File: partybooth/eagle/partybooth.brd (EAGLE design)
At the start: 61.6 x 39 mm, 26 parts, among them IC1 TINY13-20PU, IC2 78L05Z, J1 Lamp, J2 Button, J3 12V, T1 2N3904, T2 2N3904, X1 1501_06

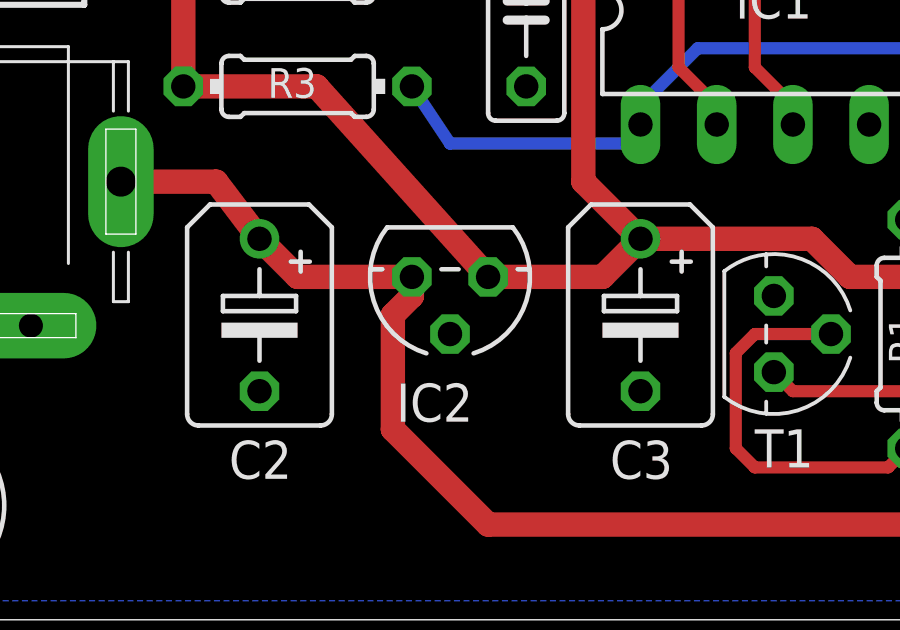
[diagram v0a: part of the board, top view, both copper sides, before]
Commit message: 
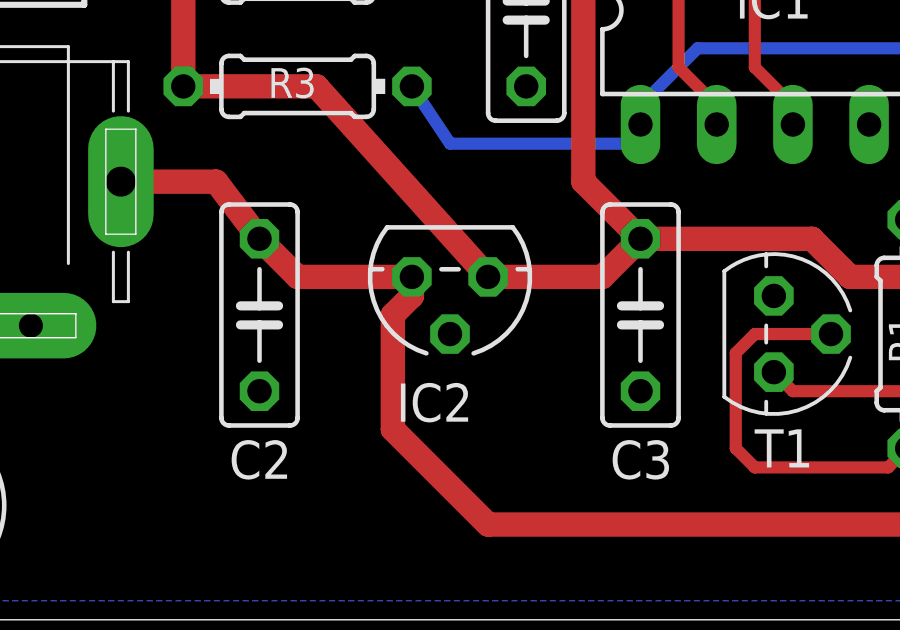
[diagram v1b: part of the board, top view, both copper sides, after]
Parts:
- C2: value 100u -> 0.33u; device rcl:B45181B -> rcl:C050-025X075
- C3: value 10u -> 0.1u; device rcl:B45181B -> rcl:C050-025X075
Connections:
- net +12V: now also C2.1; no longer C2.+
- net +5V: now also C3.1; no longer C3.+
- net GND: now also C2.2, C3.2; no longer C2.-, C3.-
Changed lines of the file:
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@@
 <attribute name="NAME" x="22.352" y="7.874" size="1.27" layer="25" ratio="10" rot="R180"/>
 </element>
-<element name="C2" library="rcl" package="B45181B" value="100u" x="15.24" y="10.16" smashed="yes" rot="R270">
+<element name="C2" library="rcl" package="C050-025X075" value="0.33u" x="15.24" y="10.16" smashed="yes" rot="R270">
 <attribute name="NAME" x="14.224" y="4.699" size="1.27" layer="25" ratio="10"/>
 </element>
-<element name="C3" library="rcl" package="B45181B" value="10u" x="27.94" y="10.16" smashed="yes" rot="R270">
+<element name="C3" library="rcl" package="C050-025X075" value="0.1u" x="27.94" y="10.16" smashed="yes" rot="R270">
 <attribute name="NAME" x="26.924" y="4.699" size="1.27" layer="25" ratio="10"/>
 </element>
@@
 <contactref element="OK1" pad="2"/>
 <contactref element="OK1" pad="3"/>
-<contactref element="C2" pad="-"/>
-<contactref element="C3" pad="-"/>
+<contactref element="C2" pad="2"/>
+<contactref element="C3" pad="2"/>
 <contactref element="IC2" pad="2"/>
 <contactref element="J3" pad="1"/>
@@
 <contactref element="SV1" pad="2"/>
 <contactref element="C1" pad="1"/>
-<contactref element="C3" pad="+"/>
+<contactref element="C3" pad="1"/>
 <contactref element="IC2" pad="1"/>
 <contactref element="R4" pad="2"/>
@@
 <signal name="+12V">
 <contactref element="J1" pad="1"/>
-<contactref element="C2" pad="+"/>
+<contactref element="C2" pad="1"/>
 <contactref element="IC2" pad="3"/>
 <contactref element="J3" pad="3"/>

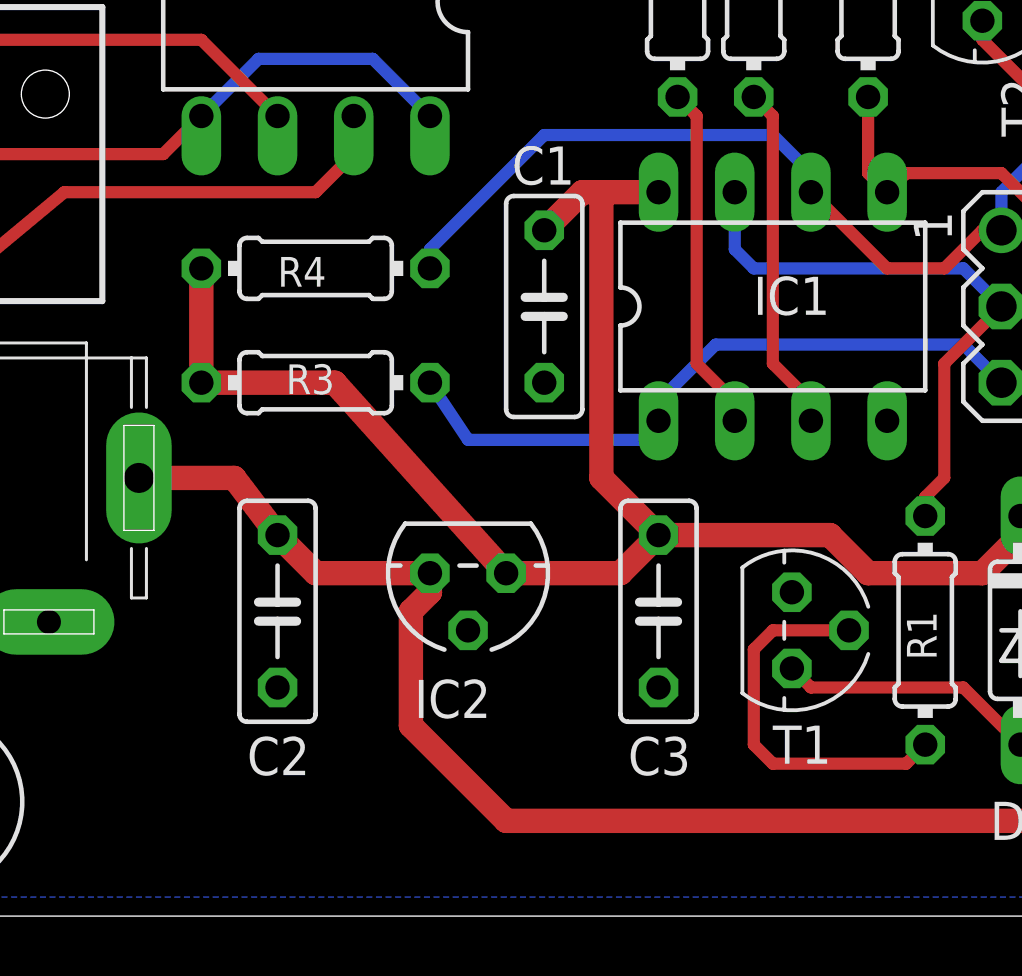
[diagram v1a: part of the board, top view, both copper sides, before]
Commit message: Check upload integrity digest, and use java.util.logging instead of System.out
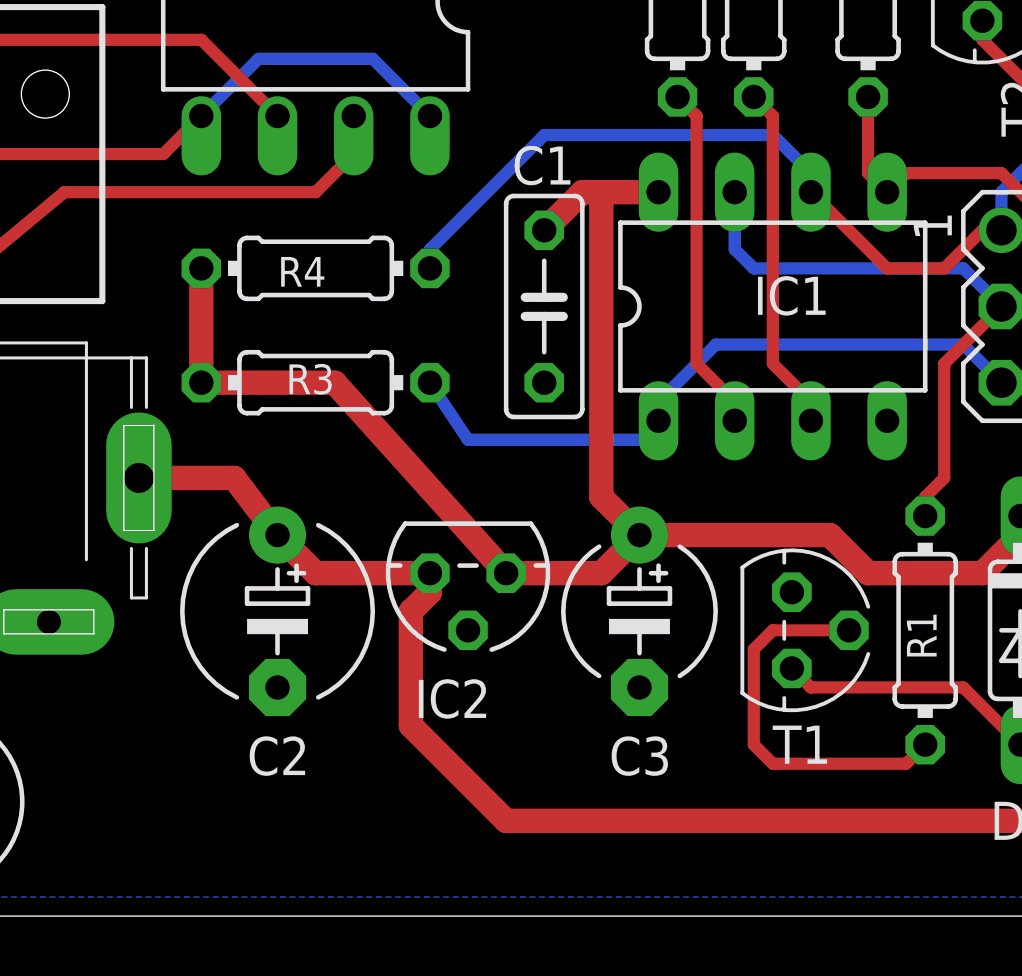
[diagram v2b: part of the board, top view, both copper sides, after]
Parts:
- C2: device rcl:C050-025X075 -> rcl:E5-6
- C3: device rcl:C050-025X075 -> rcl:E5-5
- moved C3 0.64 mm to (27.3, 10.2)
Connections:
- net +12V: now also C2.+; no longer C2.1
- net +5V: now also C3.+; no longer C3.1
- net GND: now also C2.-, C3.-; no longer C2.2, C3.2
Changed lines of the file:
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@@
 <?xml version="1.0" encoding="utf-8"?>
 <!DOCTYPE eagle SYSTEM "eagle.dtd">
-<eagle version="6.1">
+<eagle version="6.2">
 <drawing>
 <settings>
@@
 <attribute name="NAME" x="22.352" y="7.874" size="1.27" layer="25" ratio="10" rot="R180"/>
 </element>
-<element name="C2" library="rcl" package="C050-025X075" value="0.33u" x="15.24" y="10.16" smashed="yes" rot="R270">
+<element name="C2" library="rcl" package="E5-6" value="0.33u" x="15.24" y="10.16" smashed="yes" rot="R270">
 <attribute name="NAME" x="14.224" y="4.699" size="1.27" layer="25" ratio="10"/>
 </element>
-<element name="C3" library="rcl" package="C050-025X075" value="0.1u" x="27.94" y="10.16" smashed="yes" rot="R270">
-<attribute name="NAME" x="26.924" y="4.699" size="1.27" layer="25" ratio="10"/>
+<element name="C3" library="rcl" package="E5-5" value="0.1u" x="27.305" y="10.16" smashed="yes" rot="R270">
+<attribute name="NAME" x="26.289" y="4.699" size="1.27" layer="25" ratio="10"/>
 </element>
 <element name="R3" library="rcl" package="0204/7" value="10k" x="16.51" y="17.78" smashed="yes" rot="R180">
@@
 <contactref element="OK1" pad="2"/>
 <contactref element="OK1" pad="3"/>
-<contactref element="C2" pad="2"/>
-<contactref element="C3" pad="2"/>
+<contactref element="C2" pad="-"/>
+<contactref element="C3" pad="-"/>
 <contactref element="IC2" pad="2"/>
 <contactref element="J3" pad="1"/>
@@
 <contactref element="SV1" pad="2"/>
 <contactref element="C1" pad="1"/>
-<contactref element="C3" pad="1"/>
+<contactref element="C3" pad="+"/>
 <contactref element="IC2" pad="1"/>
 <contactref element="R4" pad="2"/>
@@
 <wire x1="17.145" y1="17.78" x2="12.7" y2="17.78" width="0.8128" layer="1"/>
 <wire x1="12.7" y1="17.78" x2="12.7" y2="21.59" width="0.8128" layer="1"/>
-<wire x1="22.86" y1="11.43" x2="26.67" y2="11.43" width="0.8128" layer="1"/>
-<wire x1="26.67" y1="11.43" x2="27.94" y2="12.7" width="0.8128" layer="1"/>
+<wire x1="22.86" y1="11.43" x2="26.035" y2="11.43" width="0.8128" layer="1"/>
+<wire x1="26.035" y1="11.43" x2="27.305" y2="12.7" width="0.8128" layer="1"/>
 <wire x1="24.13" y1="22.86" x2="25.4" y2="24.13" width="0.8128" layer="1"/>
 <wire x1="25.4" y1="24.13" x2="26.035" y2="24.13" width="0.8128" layer="1"/>
 <wire x1="26.035" y1="24.13" x2="27.94" y2="24.13" width="0.8128" layer="1"/>
-<wire x1="27.94" y1="12.7" x2="26.035" y2="14.605" width="0.8128" layer="1"/>
-<wire x1="26.035" y1="14.605" x2="26.035" y2="24.13" width="0.8128" layer="1"/>
-<wire x1="27.94" y1="12.7" x2="33.655" y2="12.7" width="0.8128" layer="1"/>
+<wire x1="27.305" y1="12.7" x2="26.035" y2="13.97" width="0.8128" layer="1"/>
+<wire x1="26.035" y1="13.97" x2="26.035" y2="24.13" width="0.8128" layer="1"/>
+<wire x1="27.305" y1="12.7" x2="33.655" y2="12.7" width="0.8128" layer="1"/>
 <wire x1="33.655" y1="12.7" x2="34.925" y2="11.43" width="0.8128" layer="1"/>
 <wire x1="34.925" y1="11.43" x2="38.735" y2="11.43" width="0.8128" layer="1"/>
@@
 <signal name="+12V">
 <contactref element="J1" pad="1"/>
-<contactref element="C2" pad="1"/>
+<contactref element="C2" pad="+"/>
 <contactref element="IC2" pad="3"/>
 <contactref element="J3" pad="3"/>

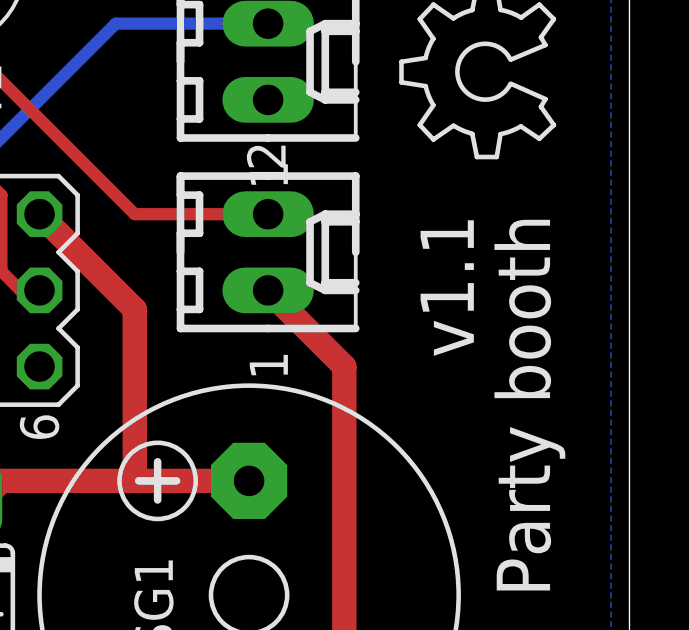
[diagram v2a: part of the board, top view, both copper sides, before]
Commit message: 
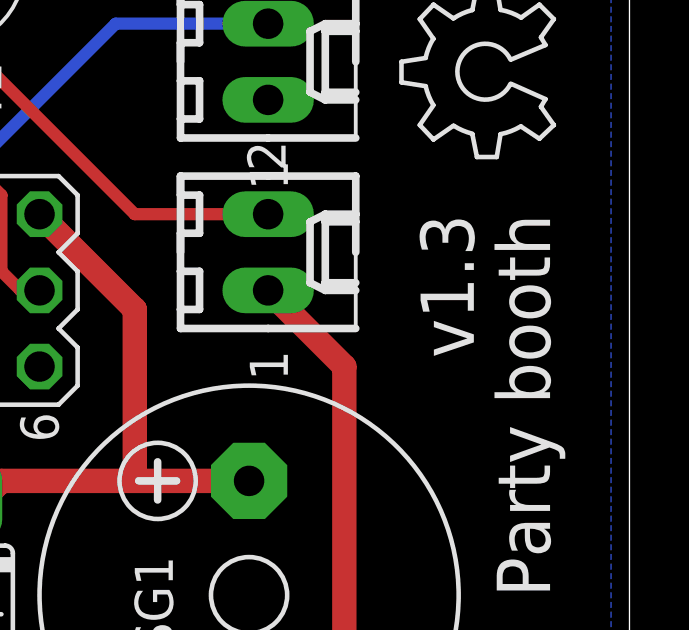
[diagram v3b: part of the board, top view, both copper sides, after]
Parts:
- C2: value 0.33u -> 100u
- C3: value 0.1u -> 10u
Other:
- board text added: "v1.3"
- board text removed: "v1.1"
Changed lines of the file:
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@@
 <wire x1="0" y1="39.04" x2="0" y2="0" width="0" layer="20"/>
 <text x="57.15" y="22.86" size="1.778" layer="21" rot="R270">Party booth</text>
-<text x="54.61" y="22.86" size="1.778" layer="21" rot="R270">v1.1</text>
+<text x="54.61" y="22.86" size="1.778" layer="21" rot="R270">v1.3</text>
 </plain>
 <attributes>
@@
 <attribute name="NAME" x="22.352" y="7.874" size="1.27" layer="25" ratio="10" rot="R180"/>
 </element>
-<element name="C2" library="rcl" package="E5-6" value="0.33u" x="15.24" y="10.16" smashed="yes" rot="R270">
+<element name="C2" library="rcl" package="E5-6" value="100u" x="15.24" y="10.16" smashed="yes" rot="R270">
 <attribute name="NAME" x="14.224" y="4.699" size="1.27" layer="25" ratio="10"/>
 </element>
-<element name="C3" library="rcl" package="E5-5" value="0.1u" x="27.305" y="10.16" smashed="yes" rot="R270">
+<element name="C3" library="rcl" package="E5-5" value="10u" x="27.305" y="10.16" smashed="yes" rot="R270">
 <attribute name="NAME" x="26.289" y="4.699" size="1.27" layer="25" ratio="10"/>
 </element>
